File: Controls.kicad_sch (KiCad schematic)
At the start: 10 parts, among them J1 BATT 3V, SW10 100k, SW5 100SP1T1B4M2QE, SW9 100SP1T1B4M2QE, U1 CD74HC4017M96, U2 LMC555CMX/NOPB

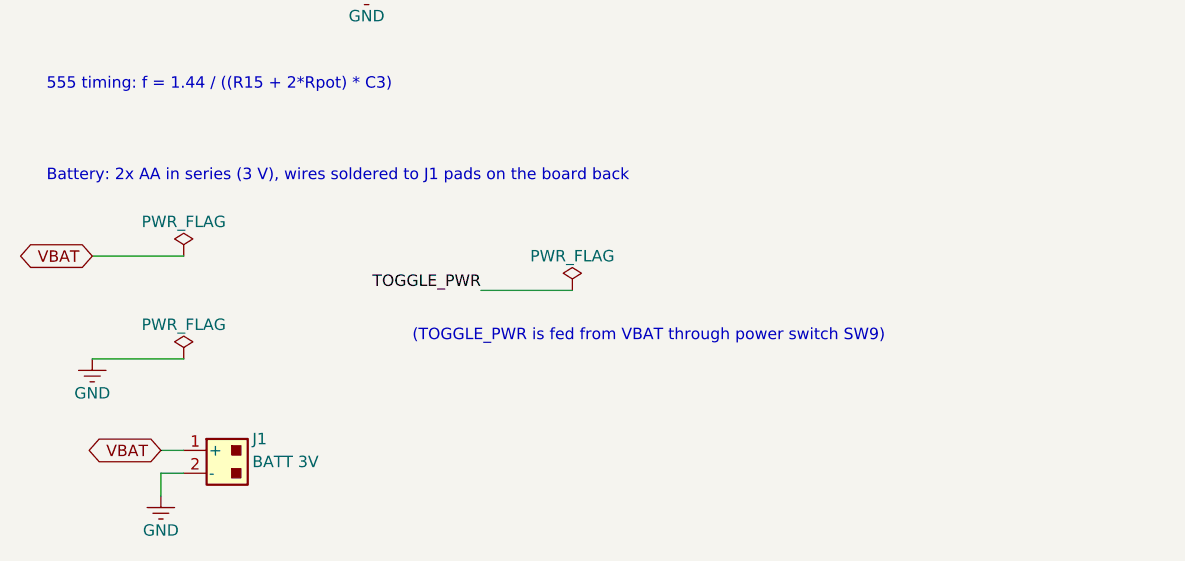
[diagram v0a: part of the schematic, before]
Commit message: Add in changes: move to 0805 parts, routing updates
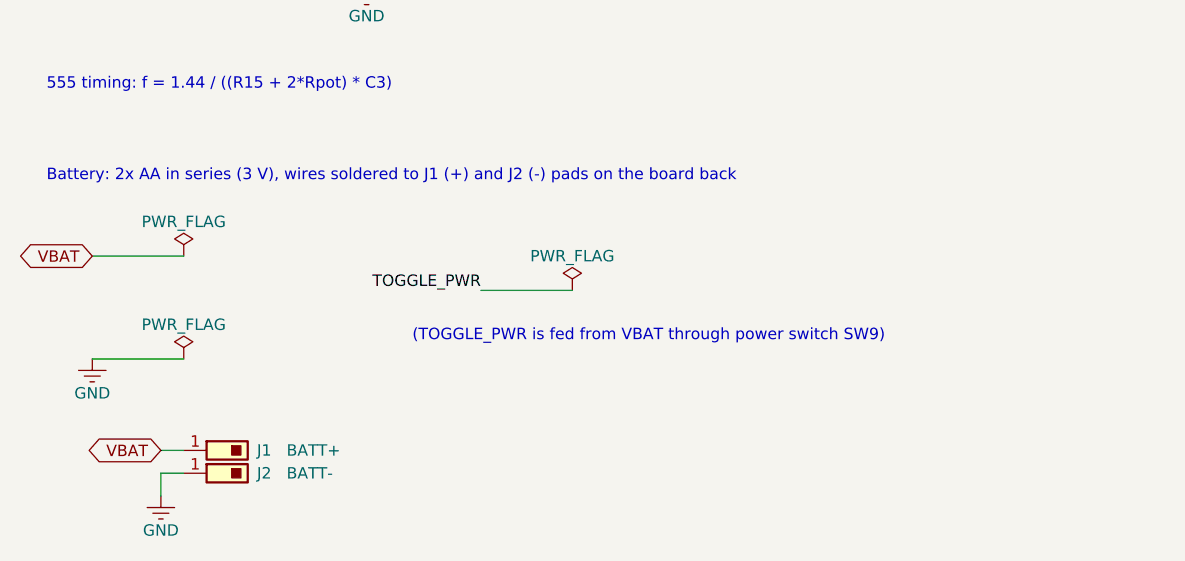
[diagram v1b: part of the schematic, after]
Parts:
- added J2: BATT-, Custom_Parts:SolderPad_1x1_8x8mm, symbol birthday:SolderPad_1x1
- C1, C2: footprint Custom_Parts:C_0402_1005Metric -> Custom_Parts:C_0805_2012Metric; symbol birthday:CC0402KRX5R7BB104 -> birthday:CC0805KRX7R9BB104; Capacitance 0.1uF 16V X5R -> 0.1uF 50V X7R; MPN CC0402KRX5R7BB104 -> CC0805KRX7R9BB104
- C3: footprint Custom_Parts:C_0402_1005Metric -> Custom_Parts:C_0805_2012Metric; symbol birthday:GRM155R61A106ME11D -> birthday:GRM21BR61E106KA73L; Capacitance 10uF 10V X5R -> 10uF 25V X5R; MPN GRM155R61A106ME11D -> GRM21BR61E106KA73L
- J1: value BATT 3V -> BATT+; footprint Custom_Parts:SolderPad_1x2_10x10mm_P12.7mm -> Custom_Parts:SolderPad_1x1_8x8mm; symbol birthday:SolderPad_1x2 -> birthday:SolderPad_1x1
- R15: footprint Custom_Parts:R_0402_1005Metric -> Custom_Parts:R_0805_2012Metric; symbol birthday:RC0402FR-07100KL -> birthday:RC0805FR-07100KL; MPN RC0402FR-07100KL -> RC0805FR-07100KL
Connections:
- net GND: now also J2.1; no longer J1.2 (-)
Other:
- note added: "Battery: 2x AA in series (3 V), wires soldered to J1 (+) and J2 (-) pads on the board back"
- note removed: "Battery: 2x AA in series (3 V), wires soldered to J1 pads on the board back"
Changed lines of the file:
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@@
 		)
 	)
-	(text "Battery: 2x AA in series (3 V), wires soldered to J1 pads on the board back"
+	(text "Battery: 2x AA in series (3 V), wires soldered to J1 (+) and J2 (-) pads on the board back"
 		(exclude_from_sim no)
 		(at 25.4 157.48 0)
@@
 	)
 	(symbol
-		(lib_id "birthday:SolderPad_1x2")
+		(lib_id "birthday:SolderPad_1x1")
 		(at 45.72 187.96 0)
 		(unit 1)
@@
 		(dnp no)
 		(property "Reference" "J1"
-			(at 48.26 186.69 0)
+			(at 48.768 187.96 0)
 			(show_name no)
 			(do_not_autoplace no)
@@
 			)
 		)
-		(property "Value" "BATT 3V"
-			(at 48.26 189.23 0)
+		(property "Value" "BATT+"
+			(at 52.07 187.96 0)
 			(show_name no)
 			(do_not_autoplace no)
@@
 			)
 		)
-		(property "Footprint" "Custom_Parts:SolderPad_1x2_10x10mm_P12.7mm"
+		(property "Footprint" "Custom_Parts:SolderPad_1x1_8x8mm"
 			(at 45.72 187.96 0)
 			(hide yes)
@@
 			)
 		)
-		(property "Description" "Two 10x10 mm rounded-square solder pads for wires (pin 1 = +, pin 2 = -)"
+		(property "Description" "Single 8x8 mm rounded-square solder pad for a wire"
 			(at 45.72 187.96 0)
 			(hide yes)
@@
 		)
 		(pin "1"
-		)
-		(pin "2"
 		)
 		(instances
@@
 				(path "/a43a4040-333c-4599-a917-1b988824fbca/68a851f1-710f-55ef-883e-1686656dbfe0"
 					(reference "J1")
+					(unit 1)
+				)
+			)
+		)
+	)
+	(symbol
+		(lib_id "birthday:SolderPad_1x1")
+		(at 45.72 190.5 0)
+		(unit 1)
+		(body_style 1)
+		(exclude_from_sim no)
+		(in_bom no)
+		(on_board yes)
+		(in_pos_files yes)
+		(dnp no)
+		(property "Reference" "J2"
+			(at 48.768 190.5 0)
+			(show_name no)
+			(do_not_autoplace no)
+			(effects
+				(font
+					(size 1.27 1.27)
+				)
+				(justify left)
+			)
+		)
+		(property "Value" "BATT-"
+			(at 52.07 190.5 0)
+			(show_name no)
+			(do_not_autoplace no)
+			(effects
+				(font
+					(size 1.27 1.27)
+				)
+				(justify left)
+			)
+		)
+		(property "Footprint" "Custom_Parts:SolderPad_1x1_8x8mm"
+			(at 45.72 190.5 0)
+			(hide yes)
+			(show_name no)
+			(do_not_autoplace no)
+			(effects
+				(font
+					(size 1.27 1.27)
+				)
+			)
+		)
+		(property "Datasheet" ""
+			(at 45.72 190.5 0)
+			(hide yes)
+			(show_name no)
+			(do_not_autoplace no)
+			(effects
+				(font
+					(size 1.27 1.27)
+				)
+			)
+		)
+		(property "Description" "Single 8x8 mm rounded-square solder pad for a wire"
+			(at 45.72 190.5 0)
+			(hide yes)
+			(show_name no)
+			(do_not_autoplace no)
+			(effects
+				(font
+					(size 1.27 1.27)
+				)
+			)
+		)
+		(pin "1"
+		)
+		(instances
+			(project "Griffin_kicad"
+				(path "/a43a4040-333c-4599-a917-1b988824fbca/68a851f1-710f-55ef-883e-1686656dbfe0"
+					(reference "J2")
 					(unit 1)
 				)
@@
 	)
 	(symbol
-		(lib_id "birthday:CC0402KRX5R7BB104")
+		(lib_id "birthday:CC0805KRX7R9BB104")
 		(at 149.86 40.64 90)
 		(unit 1)
@@
 			)
 		)
-		(property "Footprint" "Custom_Parts:C_0402_1005Metric"
+		(property "Footprint" "Custom_Parts:C_0805_2012Metric"
 			(at 149.86 40.64 270)
 			(hide yes)
@@
 			)
 		)
-		(property "Datasheet" "https://www.yageo.com/en/ProductSearch/PartNumberSearch?part_number=CC0402KRX5R7BB104"
+		(property "Datasheet" "https://www.yageo.com/en/ProductSearch/PartNumberSearch?part_number=CC0805KRX7R9BB104"
 			(at 149.86 40.64 270)
 			(hide yes)
@@
 			)
 		)
-		(property "Description" "Capacitor, MLCC, 0.1uF, 16V, 10%, X5R, 0402"
+		(property "Description" "Capacitor, MLCC, 0.1uF, 50V, 10%, X7R, 0805"
 			(at 149.86 40.64 270)
 			(hide yes)
@@
 			)
 		)
-		(property "MPN" "CC0402KRX5R7BB104"
+		(property "MPN" "CC0805KRX7R9BB104"
 			(at 149.86 40.64 270)
 			(hide yes)
@@
 			)
 		)
-		(property "Capacitance" "0.1uF 16V X5R"
+		(property "Capacitance" "0.1uF 50V X7R"
 			(at 149.86 40.64 270)
 			(hide yes)
@@
 	)
 	(symbol
-		(lib_id "birthday:CC0402KRX5R7BB104")
+		(lib_id "birthday:CC0805KRX7R9BB104")
 		(at 68.58 45.72 90)
 		(unit 1)
@@
 			)
 		)
-		(property "Footprint" "Custom_Parts:C_0402_1005Metric"
+		(property "Footprint" "Custom_Parts:C_0805_2012Metric"
 			(at 68.58 45.72 270)
 			(hide yes)
@@
 			)
 		)
-		(property "Datasheet" "https://www.yageo.com/en/ProductSearch/PartNumberSearch?part_number=CC0402KRX5R7BB104"
+		(property "Datasheet" "https://www.yageo.com/en/ProductSearch/PartNumberSearch?part_number=CC0805KRX7R9BB104"
 			(at 68.58 45.72 270)
 			(hide yes)
@@
 			)
 		)
-		(property "Description" "Capacitor, MLCC, 0.1uF, 16V, 10%, X5R, 0402"
+		(property "Description" "Capacitor, MLCC, 0.1uF, 50V, 10%, X7R, 0805"
 			(at 68.58 45.72 270)
 			(hide yes)
@@
 			)
 		)
-		(property "MPN" "CC0402KRX5R7BB104"
+		(property "MPN" "CC0805KRX7R9BB104"
 			(at 68.58 45.72 270)
 			(hide yes)
@@
 			)
 		)
-		(property "Capacitance" "0.1uF 16V X5R"
+		(property "Capacitance" "0.1uF 50V X7R"
 			(at 68.58 45.72 270)
 			(hide yes)
@@
 	)
 	(symbol
-		(lib_id "birthday:RC0402FR-07100KL")
+		(lib_id "birthday:RC0805FR-07100KL")
 		(at 50.8 104.14 180)
 		(unit 1)
@@
 			)
 		)
-		(property "Footprint" "Custom_Parts:R_0402_1005Metric"
+		(property "Footprint" "Custom_Parts:R_0805_2012Metric"
 			(at 50.8 104.14 0)
 			(hide yes)
@@
 			)
 		)
-		(property "Datasheet" "https://www.yageo.com/en/ProductSearch/PartNumberSearch?part_number=RC0402FR-07100KL"
+		(property "Datasheet" "https://www.yageo.com/en/ProductSearch/PartNumberSearch?part_number=RC0805FR-07100KL"
 			(at 50.8 104.14 0)
 			(hide yes)
@@
 			)
 		)
-		(property "Description" "Resistor, 100k, 1%, 62.5mW, 50V, 100ppm/C, Thick Film, 0402"
+		(property "Description" "Resistor, 100k, 1%, 125mW, 150V, 100ppm/C, Thick Film, 0805"
 			(at 50.8 104.14 0)
 			(hide yes)
@@
 			)
 		)
-		(property "MPN" "RC0402FR-07100KL"
+		(property "MPN" "RC0805FR-07100KL"
 			(at 50.8 104.14 0)
 			(hide yes)
@@
 	)
 	(symbol
-		(lib_id "birthday:GRM155R61A106ME11D")
+		(lib_id "birthday:GRM21BR61E106KA73L")
 		(at 60.96 129.54 0)
 		(unit 1)
@@
 			)
 		)
-		(property "Footprint" "Custom_Parts:C_0402_1005Metric"
+		(property "Footprint" "Custom_Parts:C_0805_2012Metric"
 			(at 60.96 129.54 0)
 			(hide yes)
@@
 			)
 		)
-		(property "Datasheet" "https://www.murata.com/en-us/products/productdetail?partno=GRM155R61A106ME11D"
+		(property "Datasheet" "https://www.murata.com/en-us/products/productdetail?partno=GRM21BR61E106KA73L"
 			(at 60.96 129.54 0)
 			(hide yes)
@@
 			)
 		)
-		(property "Description" "Capacitor, MLCC, 10uF, 10V, 20%, X5R, 0402 (0.7mm max height)"
+		(property "Description" "Capacitor, MLCC, 10uF, 25V, 10%, X5R, 0805 (1.25mm nominal height)"
 			(at 60.96 129.54 0)
 			(hide yes)
@@
 			)
 		)
-		(property "MPN" "GRM155R61A106ME11D"
+		(property "MPN" "GRM21BR61E106KA73L"
 			(at 60.96 129.54 0)
 			(hide yes)
@@
 			)
 		)
-		(property "Capacitance" "10uF 10V X5R"
+		(property "Capacitance" "10uF 25V X5R"
 			(at 60.96 129.54 0)
 			(hide yes)

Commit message: Add in final updates
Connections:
- net DISCHARGE: now also SW10.3; no longer SW10.1
